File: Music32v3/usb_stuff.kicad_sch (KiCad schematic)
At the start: 0 parts

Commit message: SD card and usb and power
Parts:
- added C12, C13, C14: 4.7uF, symbol Device:C_Small
- added C17, C19, C20, C28, C29, C30, C31, C32, C33: 1uF, symbol Device:C_Small
- added C21, C22: 24pF, symbol Device:C_Small
- added C23, C24: 0.1uF, symbol Device:C_Small
- added C38: 100nF, Capacitor_SMD:C_0402_1005Metric, symbol Device:C_Small
- added D3: LED, symbol Device:LED
- added FB1: 100ohm@100MHz, symbol Device:FerriteBead_Small
- added J3: Micro_SD_Card_Det1, symbol Connector:Micro_SD_Card_Det1
- added Q2 (x2): CJ3134K KF, symbol Device:Q_NMOS_GSD
- added Q4: CJ3139K, symbol Device:Q_PMOS_GSD
- added R19: 4K7, symbol Device:R_Small
- added R20: DNP, symbol Device:R_Small
- added R23: 1M, Resistor_SMD:R_0402_1005Metric, symbol Device:R_Small
- added R37: 100K, Resistor_SMD:R_0402_1005Metric, symbol Device:R
- added R38, R39, R40: DNP, Resistor_SMD:R_0402_1005Metric, symbol Device:R
- added R8: 2K, symbol Device:R
- added U10, U11, U12: TPD2EUSB30, Package_TO_SOT_SMD:Texas_DRT-3, symbol Power_Protection:TPD2EUSB30
- added U13, U14, U15, U16, U17, U19: SN74LVC1G3157, symbol sn74lvc1g3157:SN74LVC1G3157
- added U18: CH340X, symbol ch340x:CH340X
- added U6: GL823, symbol gl823:GL823
- added U7: ~, symbol sl2-1s:SL2-1s
- added Y1: 12MHz, symbol Device:Crystal_GND24_Small
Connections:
- new net: C21.2, U7.12 (XIN), Y1.1
- new net: R8.1, U6.12 (LED)
- new net: C12.1, FB1.1, U6.13 (AVDD)
- new net: C19.1, U7.10 (VDD18)
- new net: C22.2, U7.11 (XOUT), Y1.3
- new net: C17.1, U7.9 (VDD33)
- new net: D3.2 (A), R8.2
- new net: C38.1, J3.4 (VDD), Q4.3 (D)
- new net: R20.1, U18.5 (CTS)
- new net: Q2.1 (G), Q2.2 (S), R19.1, R20.2, U18.6 (TNOW/DTR)
- new net: Q2.1 (G), Q2.2 (S), U18.4 (RTS)
- new net +3.3V: R37.1, R38.1, R39.1, R40.1
- new net +3V3: C28.1, C29.1, C30.1, C31.1, C32.1, C33.1, Q4.2 (S), R23.2, U13.5 (VCC), U14.5 (VCC), U15.5 (VCC), U16.5 (VCC), U17.5 (VCC), U19.5 (VCC)
- new net CLK: U11.2 (D-)
- new net CLK_RD: U17.1 (B2), U6.4 (CLK)
- new net CLK_SD: J3.5 (CLK), U17.4 (A)
- new net CLK_SD_UC: R38.2, U17.3 (B1)
- new net CMD_RD: U19.1 (B2), U6.5 (CMD)
- new net CMD/MOSI: U11.1 (D+)
- new net CMD/MOSI_SD: J3.3 (CMD), U19.4 (A)
- new net CS_SD: R37.2, U13.3 (B1)
- new net D+: U7.6 (UDP)
- new net D-: U7.5 (UDM)
- new net DAT0_RD: U16.1 (B2), U6.3 (D0)
- new net DAT0/MISO: U12.1 (D+)
- new net DAT0/MISO_SD: J3.7 (DAT0), U16.4 (A)
- new net DAT1: U12.2 (D-)
- new net DAT1_RD: U15.1 (B2), U6.2 (D1)
- new net DAT1_SD: J3.8 (DAT1), U15.4 (A)
- new net DAT2: U10.2 (D-)
- new net DAT2_RD: U14.1 (B2), U6.7 (D2)
- new net DAT2_SD: J3.1 (DAT2), U14.4 (A)
- new net DAT3_RD: U13.1 (B2), U6.6 (D3)
- new net DAT3/CS: U10.1 (D+)
- new net DAT3/CS_SD: J3.2 (DAT3/CD), U13.4 (A)
- new net DVDD: C13.1, C23.1, C24.1, FB1.2, U18.10 (V3), U18.7 (VCC), U6.9 (DVDD)
- new net EN: Q2.3 (D)
- new net GND: C12.2, C13.2, C14.2, C17.2, C19.2, C20.2, C21.1, C22.1, C23.2, C24.2, C28.2, C29.2, C30.2, C31.2, C32.2, C33.2, C38.2, D3.1 (K), J3.10 (SHIELD), J3.6 (VSS), R19.2, U10.3 (GND), U11.3 (GND), U12.3 (GND), U13.2 (GND), U14.2 (GND), U15.2 (GND), U16.2 (GND), U17.2 (GND), U18.3 (GND), U19.2 (GND), U6.1 (GND), U6.11 (GPIO), U6.14 (GND), U7.8 (VSS), Y1.2, Y1.4
- new net IO0: Q2.3 (D)
- new net MOSI_SD: R40.2, U19.3 (B1)
- new net RXD: U18.9 (RXD)
- new net SD_D+: U6.15 (D+)
- new net SD_D-: U6.16 (D-)
- new net SD_DETECT: J3.9 (DET)
- new net SD_MISO: R39.2, U16.3 (B1)
- new net SD_PWR_EN: Q4.1 (G), R23.1
- new net SD_SELECT: U13.6 (S), U14.6 (S), U15.6 (S), U16.6 (S), U17.6 (S), U19.6 (S)
- new net TXD: U18.8 (TXD)
- new net UART_D+: U18.1 (D+)
- new net UART_D-: U18.2 (D-)
- new net VBUS: C14.1, C20.1, U6.10 (VBUS), U7.7 (VDD5)
- no-connect marks 0 -> 3
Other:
- note added: "100ohm @100MHz"
- note added: "Analog switches for SD card data lines"
- note added: "Change according to pcb"
- note added: "Confirm this circuit works"
- note added: "Make switches switch to esp by defualt so when esp doesnt have power but usb is connected the reader chip cant mess with the unpowered sd however the switches will be unpowered aswell, though this should only be a bug for development as the power switch isnt intended for final use"
- note added: "Only way to be able to switch between SD mode and spi mode is power cycle"
- note added: "SD card w/ protection diodes"
- note added: "SL2-1s"
- note added: "USB SD card reader"
- note added: "USB hub"
- note added: "USB to UART converter"
- note added: "USB to UART feeds from SD card reader regulator 3.3V"
- note added: "X322512MOB4SI"
- note added: "open source by default place cts resistor and remove pulldown for push pull"

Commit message: Schematic
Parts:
- C12, C13, C14, C17, C19, C20, C21, C22, C23, C24, C28, C29, C30, C31, C32, C33: footprint (none) -> Capacitor_SMD:C_0402_1005Metric
- C38: value 100nF -> 1uF
- D3: footprint (none) -> LED_SMD:LED_0603_1608Metric
- FB1, R19, R20, R8: footprint (none) -> Resistor_SMD:R_0402_1005Metric
- J3: footprint (none) -> Music:MOLEX_503398-1892
- Q2, Q4: footprint (none) -> Package_TO_SOT_SMD:SOT-723
- U13, U14, U15, U16, U17, U19: footprint (none) -> Package_TO_SOT_SMD:SOT-363_SC-70-6
- U18: footprint (none) -> Package_SO:MSOP-10_3x3mm_P0.5mm
- U6: footprint (none) -> Package_SO:SSOP-16_3.9x4.9mm_P0.635mm
- U7: footprint (none) -> Music:SL2.1S
- Y1: footprint (none) -> Crystal:Crystal_SMD_2520-4Pin_2.5x2.0mm
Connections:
- net CLK_SD_UC renamed CLK_UC
- net MOSI_SD renamed MOSI_UC
- net SD_MISO renamed MISO_UC
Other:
- note added: "TXM12M0004252DBCEO00T"
- note removed: "Make switches switch to esp by defualt so when esp doesnt have power but usb is connected the reader chip cant mess with the unpowered sd however the switches will be unpowered aswell, though this should only be a bug for development as the power switch isnt intended for final use"
- note removed: "X322512MOB4SI"
- moved on the sheet: C28, C29, C30, C31, C32, C33, R37, R38, R39, R40, U13, U14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

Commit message: Reorganised
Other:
- moved on the sheet: C28, C29, C30, R37, R40, U13, U14, U19

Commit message: Auto programming
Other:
- note added: ">> happens in 1ms 1ms delay between en high and start"
- note added: "Both setups should work"
- note added: "DTR High RTS Low - EN Low IO0 High (Body diode pulls IO0 high but no difference?) DTR Low RTS High - EN HIGH IO0 Low (body diode no difference) DTR Low RTS Low - EN HIGH IO0 LOW DTR HIGH RTS HIGH - EN HIGH IO0 HIGH (Body diode pulls IO0 high)"
- note added: "DTR RTS EN IO0 1 1 1 1 0 0 1 0 1 0 0 1 0 1 1 0"
- note added: "EN LOW IO0 HIGH > EN HIGH IO0 LOW >> EN HIGH IO0 LOW"
- note added: "RTS LOW DTR HIGH > RTS LOW DTR LOW >> RTS HIGH DTR LOW"
- note added: "So its in reset then exits reset but before it starts the io0 line goes low so it starts in boot mode"
- note added: "Transistor EN LOW IO0 HIGH > EN HIGH IO0 HIGH >> EN HIGH IO0 LOW"

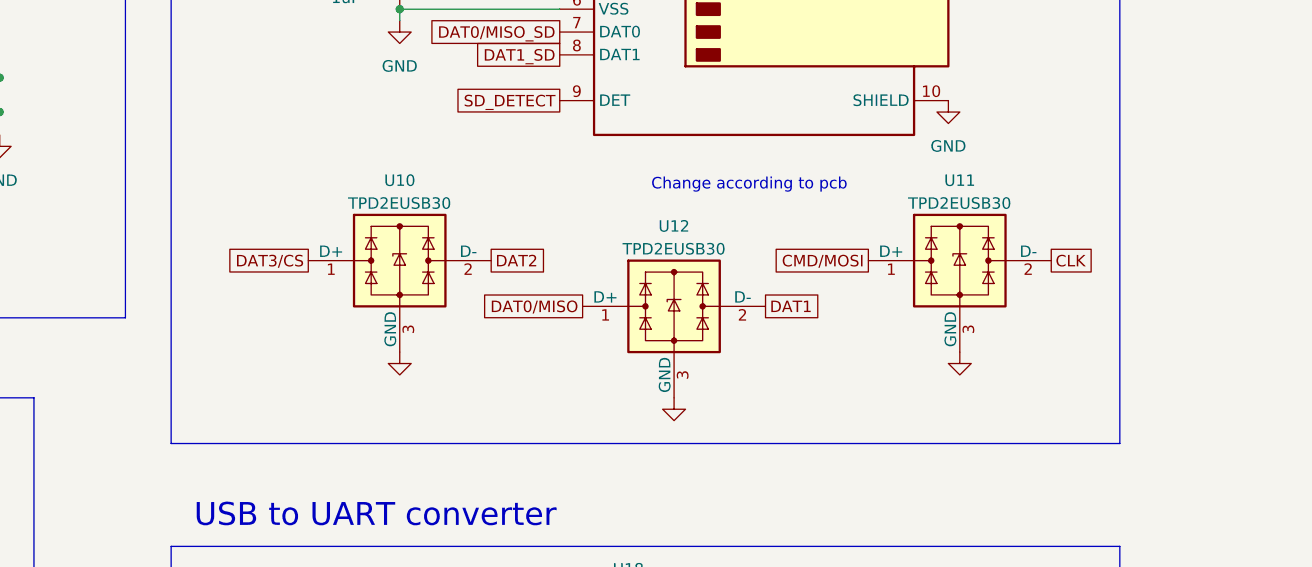
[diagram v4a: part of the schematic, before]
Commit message: PCB outline
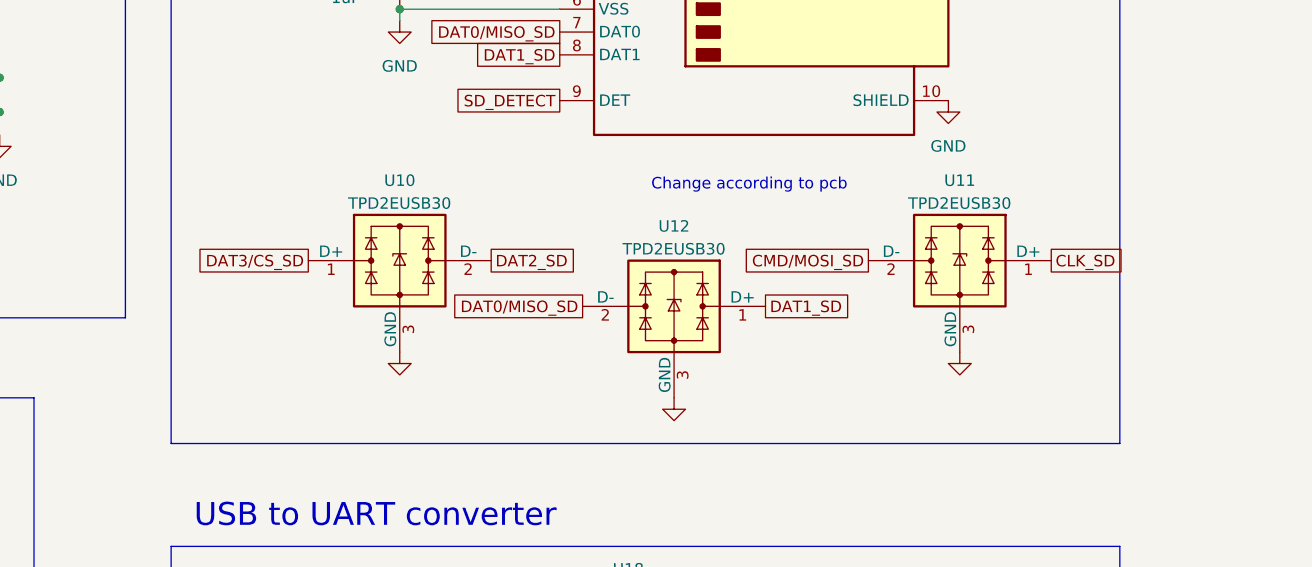
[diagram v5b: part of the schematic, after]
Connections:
- net CLK is gone; now on net CMD/MOSI_SD: U11.2 (D-)
- net CMD/MOSI is gone; now on net CLK_SD: U11.1 (D+)
- net DAT0/MISO is gone; now on net DAT1_SD: U12.1 (D+)
- net DAT1 is gone; now on net DAT0/MISO_SD: U12.2 (D-)
- net DAT2 is gone; now on net DAT2_SD: U10.2 (D-)
- net DAT3/CS is gone; now on net DAT3/CS_SD: U10.1 (D+)
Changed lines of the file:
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@@
-    )
-  )
-  (global_label "DAT0{slash}MISO" (shape passive) (at 220.98 88.9 180) (fields_autoplaced)
-    (effects (font (size 1.27 1.27)) (justify right))
-    (property "Intersheetrefs" "${INTERSHEET_REFS}" (at 208.7231 88.9 0)
-      (effects (font (size 1.27 1.27)) (justify right) hide)
     )
   )
@@
     )
   )
+  (global_label "DAT1_SD" (shape passive) (at 241.3 88.9 0) (fields_autoplaced)
+    (effects (font (size 1.27 1.27)) (justify left))
+    (property "Intersheetrefs" "${INTERSHEET_REFS}" (at 251.0773 88.9 0)
+      (effects (font (size 1.27 1.27)) (justify left) hide)
+    )
+  )
   (global_label "DAT2_SD" (shape passive) (at 218.44 43.18 180) (fields_autoplaced)
     (effects (font (size 1.27 1.27)) (justify right))
@@
     )
   )
+  (global_label "DAT3{slash}CS_SD" (shape passive) (at 190.5 83.82 180) (fields_autoplaced)
+    (effects (font (size 1.27 1.27)) (justify right))
+    (property "Intersheetrefs" "${INTERSHEET_REFS}" (at 176.9127 83.82 0)
+      (effects (font (size 1.27 1.27)) (justify right) hide)
+    )
+  )
+  (global_label "CLK_SD" (shape passive) (at 273.05 83.82 0) (fields_autoplaced)
+    (effects (font (size 1.27 1.27)) (justify left))
+    (property "Intersheetrefs" "${INTERSHEET_REFS}" (at 281.8597 83.82 0)
+      (effects (font (size 1.27 1.27)) (justify left) hide)
+    )
+  )
   (global_label "SD_D-" (shape passive) (at 80.01 35.56 0) (fields_autoplaced)
     (effects (font (size 1.27 1.27)) (justify left))
@@
     )
   )
-  (global_label "DAT3{slash}CS" (shape passive) (at 190.5 83.82 180) (fields_autoplaced)
-    (effects (font (size 1.27 1.27)) (justify right))
-    (property "Intersheetrefs" "${INTERSHEET_REFS}" (at 180.3598 83.82 0)
-      (effects (font (size 1.27 1.27)) (justify right) hide)
-    )
-  )
-  (global_label "DAT2" (shape passive) (at 210.82 83.82 0) (fields_autoplaced)
-    (effects (font (size 1.27 1.27)) (justify left))
-    (property "Intersheetrefs" "${INTERSHEET_REFS}" (at 217.1502 83.82 0)
-      (effects (font (size 1.27 1.27)) (justify left) hide)
-    )
-  )
   (global_label "SD_D+" (shape passive) (at 80.01 33.02 0) (fields_autoplaced)
     (effects (font (size 1.27 1.27)) (justify left))
@@
     )
   )
-  (global_label "CLK" (shape passive) (at 273.05 83.82 0) (fields_autoplaced)
-    (effects (font (size 1.27 1.27)) (justify left))
-    (property "Intersheetrefs" "${INTERSHEET_REFS}" (at 278.4126 83.82 0)
-      (effects (font (size 1.27 1.27)) (justify left) hide)
-    )
-  )
   (global_label "CLK_RD" (shape passive) (at 156.21 31.75 0) (fields_autoplaced)
     (effects (font (size 1.27 1.27)) (justify left))
@@
     )
   )
-  (global_label "CMD{slash}MOSI" (shape passive) (at 252.73 83.82 180) (fields_autoplaced)
-    (effects (font (size 1.27 1.27)) (justify right))
-    (property "Intersheetrefs" "${INTERSHEET_REFS}" (at 241.0174 83.82 0)
-      (effects (font (size 1.27 1.27)) (justify right) hide)
-    )
-  )
   (global_label "DAT2_RD" (shape passive) (at 52.07 129.54 0) (fields_autoplaced)
     (effects (font (size 1.27 1.27)) (justify left))
@@
     )
   )
-  (global_label "DAT1" (shape passive) (at 241.3 88.9 0) (fields_autoplaced)
-    (effects (font (size 1.27 1.27)) (justify left))
-    (property "Intersheetrefs" "${INTERSHEET_REFS}" (at 247.6302 88.9 0)
-      (effects (font (size 1.27 1.27)) (justify left) hide)
-    )
-  )
   (global_label "DAT2_SD" (shape passive) (at 36.83 124.46 180) (fields_autoplaced)
     (effects (font (size 1.27 1.27)) (justify right))
@@
     )
   )
+  (global_label "DAT2_SD" (shape passive) (at 210.82 83.82 0) (fields_autoplaced)
+    (effects (font (size 1.27 1.27)) (justify left))
+    (property "Intersheetrefs" "${INTERSHEET_REFS}" (at 220.5973 83.82 0)
+      (effects (font (size 1.27 1.27)) (justify left) hide)
+    )
+  )
   (global_label "CMD{slash}MOSI_SD" (shape passive) (at 218.44 48.26 180) (fields_autoplaced)
     (effects (font (size 1.27 1.27)) (justify right))
@@
     )
   )
+  (global_label "DAT0{slash}MISO_SD" (shape passive) (at 220.98 88.9 180) (fields_autoplaced)
+    (effects (font (size 1.27 1.27)) (justify right))
+    (property "Intersheetrefs" "${INTERSHEET_REFS}" (at 205.276 88.9 0)
+      (effects (font (size 1.27 1.27)) (justify right) hide)
+    )
+  )
   (global_label "DAT1_SD" (shape passive) (at 218.44 60.96 180) (fields_autoplaced)
     (effects (font (size 1.27 1.27)) (justify right))
@@
     (effects (font (size 1.27 1.27)) (justify right))
     (property "Intersheetrefs" "${INTERSHEET_REFS}" (at 115.106 46.99 0)
+      (effects (font (size 1.27 1.27)) (justify right) hide)
+    )
+  )
+  (global_label "CMD{slash}MOSI_SD" (shape passive) (at 252.73 83.82 180) (fields_autoplaced)
+    (effects (font (size 1.27 1.27)) (justify right))
+    (property "Intersheetrefs" "${INTERSHEET_REFS}" (at 237.5703 83.82 0)
       (effects (font (size 1.27 1.27)) (justify right) hide)
     )
@@
   )
   (symbol (lib_id "Power_Protection:TPD2EUSB30") (at 200.66 83.82 0) (unit 1)
-    (in_bom yes) (on_board yes) (dnp no) (fields_autoplaced)
+    (in_bom yes) (on_board yes) (dnp no)
     (property "Reference" "U10" (at 200.66 74.93 0)
       (effects (font (size 1.27 1.27)))
@@
     )
   )
-  (symbol (lib_id "Power_Protection:TPD2EUSB30") (at 231.14 88.9 0) (unit 1)
-    (in_bom yes) (on_board yes) (dnp no) (fields_autoplaced)
+  (symbol (lib_id "Power_Protection:TPD2EUSB30") (at 231.14 88.9 0) (mirror y) (unit 1)
+    (in_bom yes) (on_board yes) (dnp no)
     (property "Reference" "U12" (at 231.14 80.01 0)
       (effects (font (size 1.27 1.27)))
@@
       (effects (font (size 1.27 1.27)))
     )
-    (property "Footprint" "Package_TO_SOT_SMD:Texas_DRT-3" (at 212.09 96.52 0)
+    (property "Footprint" "Package_TO_SOT_SMD:Texas_DRT-3" (at 250.19 96.52 0)
       (effects (font (size 1.27 1.27)) hide)
     )
@@
     )
   )
-  (symbol (lib_id "Power_Protection:TPD2EUSB30") (at 262.89 83.82 0) (unit 1)
+  (symbol (lib_id "Power_Protection:TPD2EUSB30") (at 262.89 83.82 0) (mirror y) (unit 1)
     (in_bom yes) (on_board yes) (dnp no)
     (property "Reference" "U11" (at 262.89 74.93 0)
@@
       (effects (font (size 1.27 1.27)))
     )
-    (property "Footprint" "Package_TO_SOT_SMD:Texas_DRT-3" (at 243.84 91.44 0)
-      (effects (font (size 1.27 1.27)) hide)
-    )
+    (property "Footprint" "Package_TO_SOT_SMD:Texas_DRT-3" (at 281.94 91.44 0)
+      (effects (font (size 1.27 1.27)) hide)
+    )

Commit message: Board setup
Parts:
- added TP6 (x6): TestPoint, TestPoint:TestPoint_Pad_D1.0mm, symbol Connector:TestPoint
- added TP6 (x3): TestPoint, TestPoint:TestPoint_Pad_D2.0mm, symbol Connector:TestPoint
- added TP6: TestPoint, TestPoint:TestPoint_Pad_D1.5mm, symbol Connector:TestPoint
- Y1: footprint Crystal:Crystal_SMD_2520-4Pin_2.5x2.0mm -> Crystal:Crystal_SMD_3225-4Pin_3.2x2.5mm
- renumbered C22 to C19, C21 to C20, C20 to C21, C30 to C22, C31 to C23, C17 to C24, C19 to C25, C29 to C26, C32 to C27, C14 to C28, C13 to C29, C28 to C30, C33 to C31, C12 to C32, C23 to C34, C24 to C35, D3 to D4, J3 to J2, Q4 to Q5, R8 to R29, R20 to R33, R19 to R34, U14 to U11, U15 to U12, U7 to U13, U13 to U14, U16 to U15, U6 to U16, U19 to U17, U17 to U18, U10 to U19, U18 to U20, U12 to U21, U11 to U22
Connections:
- net +3.3V is gone; now on net +3V3: R37.1, R38.1, R39.1, R40.1
- net CLK_SD: now also TP6.1
- net CMD/MOSI_SD: now also TP6.1
- net DAT0/MISO_SD: now also TP6.1
- net DAT1_SD: now also TP6.1
- net DAT2_SD: now also TP6.1
- net DAT3/CS_SD: now also TP6.1
- net DVDD: now also TP6.1
- net SD_D+: now also U13.16 (DP3)
- net SD_D-: now also U13.15 (DM3)
- net SD_DETECT: now also TP6.1
- net SD_PWR_EN: now also TP6.1
- net UART_D+: now also U13.14 (DP4)
- net UART_D-: now also U13.13 (DM4)
- net at C38.1, J2.4 (VDD), Q5.3 (D): now also TP6.1
- net TXD renamed MCLK_TXD
- no-connect marks 3 -> 7
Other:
- note added: "TAXM12M4RFBCCT2T"
- note removed: "Confirm this circuit works"
- note removed: "TXM12M0004252DBCEO00T"
- moved on the sheet: C28, C29, C32, D4, FB1, R29, U16

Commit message: pcb done
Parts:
- R37: value 100K -> 1M
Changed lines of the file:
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@@
       (effects (font (size 1.27 1.27)))
     )
-    (property "Value" "100K" (at 102.87 115.57 0)
+    (property "Value" "1M" (at 102.87 115.57 0)
       (effects (font (size 1.27 1.27)))
     )
